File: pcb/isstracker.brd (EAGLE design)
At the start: 68.6 x 54.3 mm, 26 parts, among them IC2 L7805CV, J1 MOTOR_RIGHT, J2 MOTOR, J3 MOTOR_LEFT, J4 DISPLAY, J5 GLOBE_RESET, J6 CONTROL, J8 UART, J9 DISTANCE, Q2 60V/32A/35mΩ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

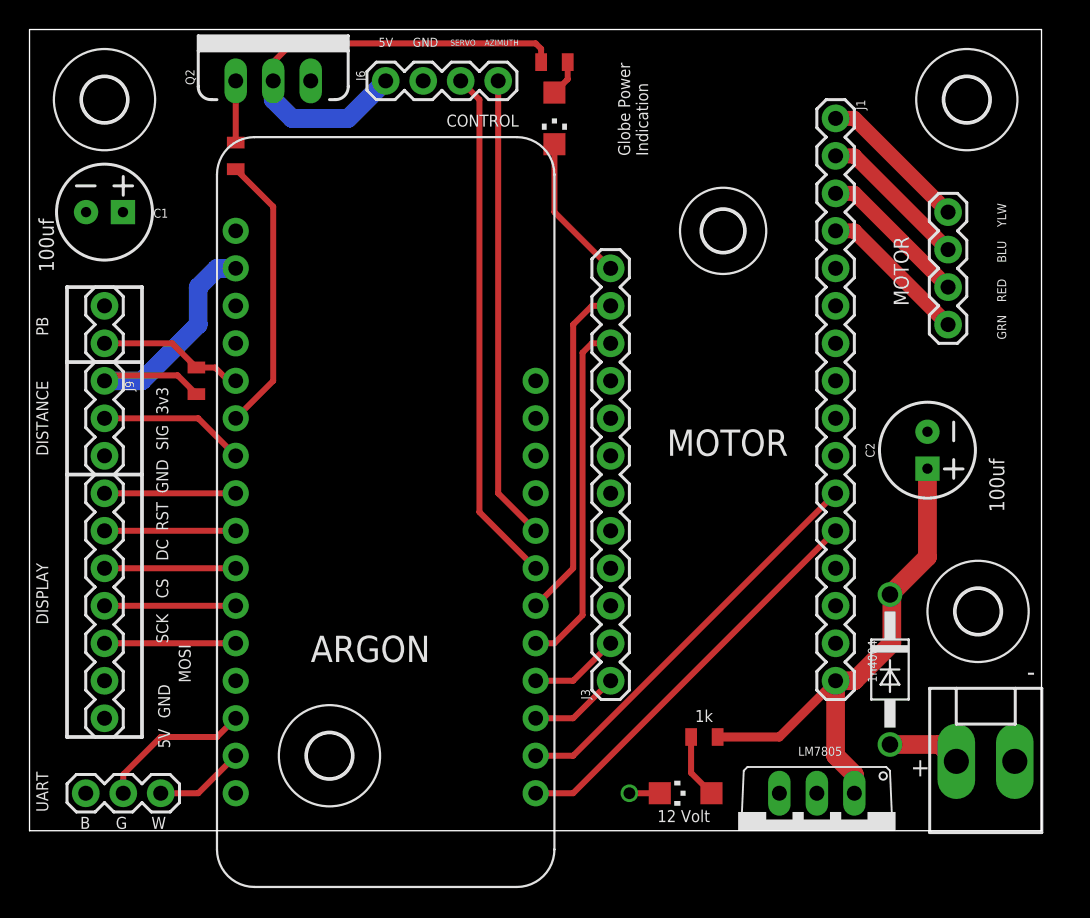
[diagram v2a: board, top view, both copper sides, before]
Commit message: Update to version 1.9
* Fix the FET, it wasn't right
* New FET in the BOM
* Put FET on low side and add pulldown on gate
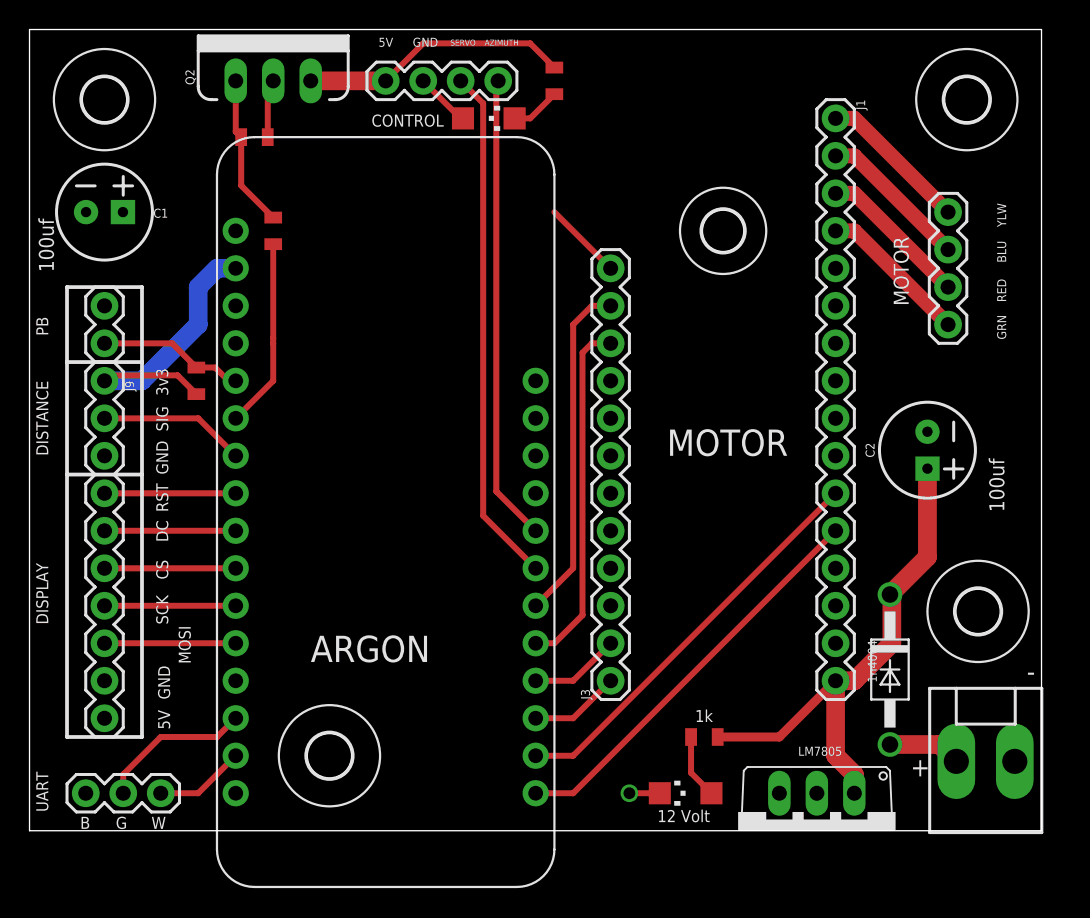
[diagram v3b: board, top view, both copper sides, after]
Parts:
- added R5: 10k, SparkFun-Resistors:0805
- Q2: value 60V/32A/35mΩ -> IRL3103PBF
- R3: value 10k -> 100
- moved R3 5.68 mm to (16.5, 40.6), turned to 90 degrees
- moved LED1 4.45 mm to (31.1, 48.3), turned to 270 degrees
- moved R2 1.27 mm to (35.6, 50.8), turned to 270 degrees
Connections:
- removed net N$3: J6.1, Q2.2, R2.1
- removed net N$6: Q2.1, R3.1
- new net N$5: Q2.1, R3.2, R5.1
- new net N$8: J6.1, Q2.3, R2.1
- net +5V: now also J6.2, LED1.A; no longer Q2.3
- net GLOBE_PWR: now also R3.1; no longer R3.2
- net GND: now also Q2.2, R5.2; no longer J6.2, LED1.C
- net N$4: now also LED1.C; no longer LED1.A
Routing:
- net N$3: track 31.5 -> 0.00 mm
- net N$8: track 0.00 -> 18.2 mm
- net N$5: track 0.00 -> 10.3 mm
- net GLOBE_PWR: track 19.0 -> 12.9 mm
- net N$6: track 4.18 -> 0.00 mm
- net +5V: track 0.00 -> 3.75 mm
- net N$4: track 2.43 -> 3.37 mm
- net GND: track 12.0 -> 11.4 mm
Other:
- board text removed: "Globe Power Indication"

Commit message: Fixes
* Add globe power using a MOSFET so the laser can be turned on/off
* Update both board layouts to accomodate new power scheme
* Fix some component positions in layout
* Migrate to screw terminals for power on board
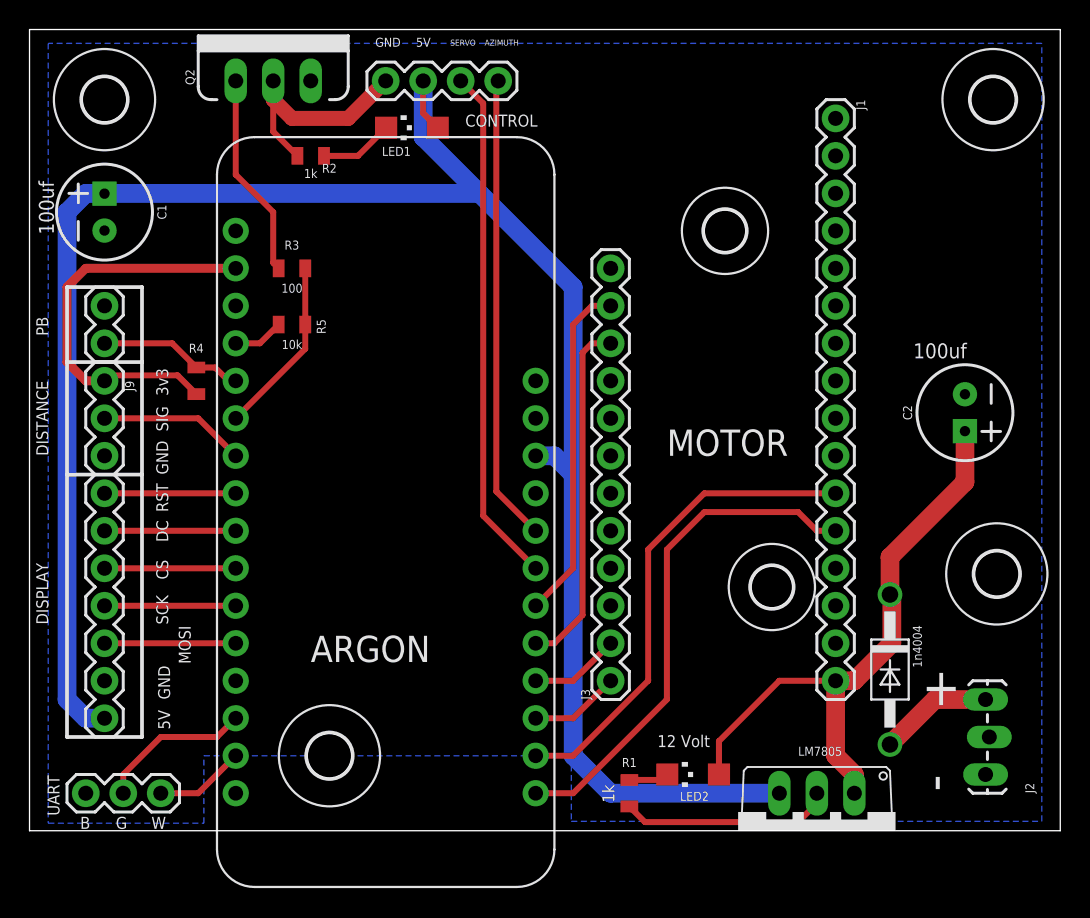
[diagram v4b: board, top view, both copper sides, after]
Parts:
- removed LED3: L171L-LPGC, adafruit:CHIPLED_1206
- removed X1: +12V, con-molex:KK-156-2
- added H5: MOUNT-HOLE2.8, holes:2,8
- added LED2: XZDG55W-3, adafruit:CHIPLED_1206
- J2: value MOTOR -> (none); device SparkFun-Connectors:1X04 -> SparkFun-Connectors:1X03_LOCK_LONGPADS
- LED1: value L171L-LPGC -> XZDG55W-3
- moved J2 30.6 mm to (64.8, 3.81)
- moved R2 17.3 mm to (19.1, 45.7), turned to 0 degrees
- moved R5 13.0 mm to (17.8, 34.3), turned to 180 degrees
- moved R1 6.35 mm to (40.6, 2.54), turned to 90 degrees
- moved LED1 5.25 mm to (25.9, 47.6), turned to 90 degrees
- moved C2 3.59 mm to (63.4, 28.3)
- moved H2 2.84 mm to (65.5, 17.4)
- moved R3 2.84 mm to (17.8, 38.1), turned to 180 degrees
- moved H3 1.78 mm to (65.3, 49.5)
- moved H6 0.13 mm to (47.1, 40.6)
- turned C1 to 90 degrees
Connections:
- removed net A+: J1.1, J2.4
- removed net A-: J1.2, J2.3
- removed net B+: J1.3, J2.2
- removed net B-: J1.4, J2.1
- removed net N$5: Q2.1, R3.2, R5.1
- new net N$3: Q2.1, R3.2
- net +12V: now also LED2.A; no longer R1.2
- net GLOBE_PWR: now also R5.1
- net GND: now also J2.1, Q2.3, R1.1; no longer LED3.C, Q2.2, X1.2
- net N$1: now also J2.3; no longer X1.1
- net N$2: now also LED2.C, R1.2; no longer LED3.A, R1.1
- net N$8: now also Q2.2; no longer Q2.3
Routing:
- net +5V: track 3.75 -> 136.2 mm
- net N$3: track 0.00 -> 13.9 mm
- net N$5: track 10.3 -> 0.00 mm
- net B-: track 10.3 -> 0.00 mm
- net B+: track 10.3 -> 0.00 mm
- net A-: track 10.3 -> 0.00 mm
- net A+: track 10.3 -> 0.00 mm
- net MTR_MS2: track 27.7 -> 34.7 mm
- net +3V3: track 20.4 -> 27.0 mm
- net GND: track 11.4 -> 17.8 mm, vias 1 -> 0
- net +12V: track 35.5 -> 41.4 mm
- net MTR_EN: track 27.7 -> 32.9 mm
- net N$1: track 4.97 -> 7.74 mm
- net N$8: track 18.2 -> 16.2 mm
- net N$2: track 4.38 -> 2.72 mm
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- added copper zone on layer 16, net GND
- removed copper zone on layer 15, net +5V
- removed copper zone on layer 2, net GND
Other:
- board size 68.6 x 54.3 mm -> 69.8 x 54.3 mm
- board text added: "ISS Position Tracker (C) Peter Buelow March, 2021 Version 1.11"
- board text added: "LED1"
- board text added: "LED2"
- board text added: "R1"
- board text added: "R2"
- board text added: "R3"
- board text added: "R4"
- board text added: "R5"
- board text removed: "BLU"
- board text removed: "GRN"
- board text removed: "ISS Position Tracker (C) Peter Buelow March, 2021 Version 1.8"
- board text removed: "RED"
- board text removed: "YLW"
